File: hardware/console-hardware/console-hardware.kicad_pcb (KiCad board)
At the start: 2 copper layers, 3 parts, among them U1 ATmega32U4-A

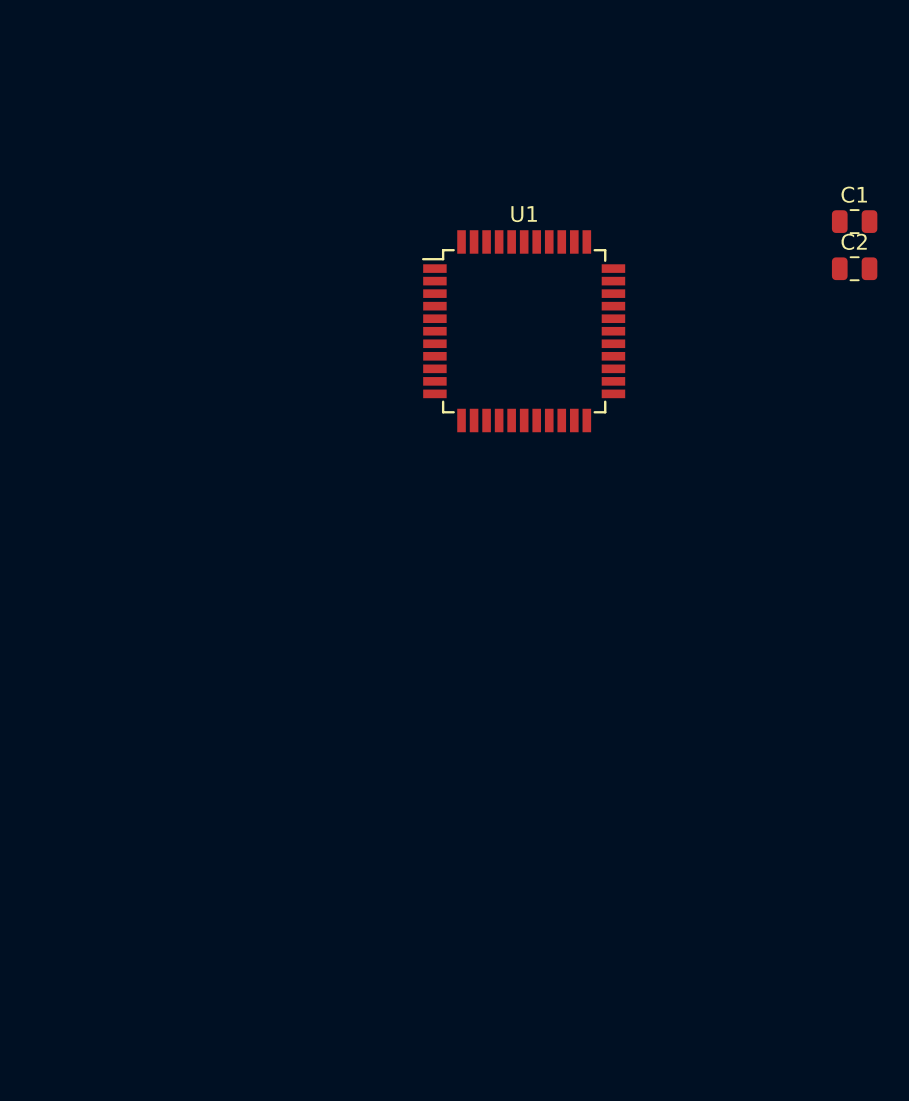
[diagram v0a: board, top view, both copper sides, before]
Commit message: Updated schematic and added preliminary layout
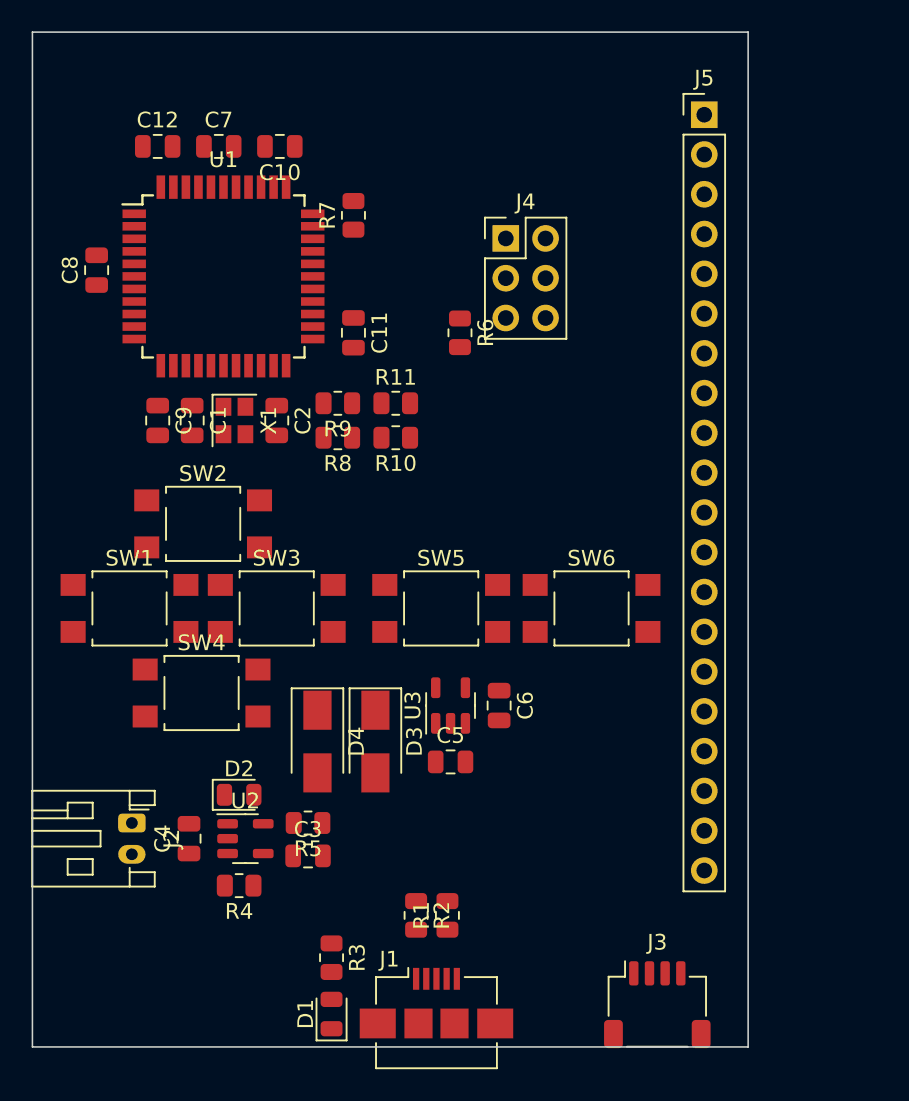
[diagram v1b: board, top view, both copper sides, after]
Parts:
- added C10: 100n, Capacitor_SMD:C_0805_2012Metric, F.Cu at (98.2, 63.7)
- added C11: 100n, Capacitor_SMD:C_0805_2012Metric, F.Cu at (102.9, 75.6)
- added C12: 100n, Capacitor_SMD:C_0805_2012Metric, F.Cu at (90.4, 63.7)
- added C3: 4.7u, Capacitor_SMD:C_0805_2012Metric, F.Cu at (100.0, 109.0)
- added C4: 4.7u, Capacitor_SMD:C_0805_2012Metric, F.Cu at (92.4, 107.9)
- added C5: 4.7u, Capacitor_SMD:C_0805_2012Metric, F.Cu at (109.1, 103.0)
- added C6: 470p, Capacitor_SMD:C_0805_2012Metric, F.Cu at (112.2, 99.4)
- added C7: 100n, Capacitor_SMD:C_0805_2012Metric, F.Cu at (94.3, 63.7)
- added C8: 1u, Capacitor_SMD:C_0805_2012Metric, F.Cu at (86.5, 71.6)
- added C9: 100n, Capacitor_SMD:C_0805_2012Metric, F.Cu at (90.4, 81.2)
- added D1: Green, LED_SMD:LED_0805_2012Metric, F.Cu at (101.5, 119.1)
- added D2: Green, LED_SMD:LED_0805_2012Metric, F.Cu at (95.6, 105.1)
- added D3: B340A, Diode_SMD:D_SMA, F.Cu at (104.3, 101.7)
- added D4: B340A, Diode_SMD:D_SMA, F.Cu at (100.6, 101.7)
- added J1: USB_B_Micro, Connector_USB:USB_Micro-B_Amphenol_10104110_Horizontal, F.Cu at (108.2, 118.4)
- added J2: LiPo battery, Connector_JST:JST_PH_S2B-PH-K_1x02_P2.00mm_Horizontal, F.Cu at (88.8, 106.9)
- added J3: Conn_01x04, Connector_JST:JST_SH_SM04B-SRSS-TB_1x04-1MP_P1.00mm_Horizontal, F.Cu at (122.3, 118.5)
- added J4: ICSP, Connector_PinHeader_2.54mm:PinHeader_2x03_P2.54mm_Vertical, F.Cu at (112.6, 69.6)
- added J5: Conn_01x20, Connector_PinHeader_2.54mm:PinHeader_1x20_P2.54mm_Vertical, F.Cu at (125.3, 61.7)
- added R1: 22, Resistor_SMD:R_0805_2012Metric, F.Cu at (108.9, 112.8)
- added R10: 0, Resistor_SMD:R_0805_2012Metric, F.Cu at (105.6, 82.3)
- added R11: 0, Resistor_SMD:R_0805_2012Metric, F.Cu at (105.6, 80.1)
- added R2: 22, Resistor_SMD:R_0805_2012Metric, F.Cu at (106.9, 112.8)
- added R3: 1k, Resistor_SMD:R_0805_2012Metric, F.Cu at (101.5, 115.5)
- added R4: 1k, Resistor_SMD:R_0805_2012Metric, F.Cu at (95.6, 110.9)
- added R5: 10k, Resistor_SMD:R_0805_2012Metric, F.Cu at (100.0, 106.9)
- added R6: 10k, Resistor_SMD:R_0805_2012Metric, F.Cu at (109.7, 75.6)
- added R7: 10k, Resistor_SMD:R_0805_2012Metric, F.Cu at (102.9, 68.1)
- added R8: 4.7k, Resistor_SMD:R_0805_2012Metric, F.Cu at (101.9, 82.3)
- added R9: 4.7k, Resistor_SMD:R_0805_2012Metric, F.Cu at (101.9, 80.1)
- added SW1: SW_Push, Button_Switch_SMD:SW_SPST_TL3305A, F.Cu at (88.6, 93.2)
- added SW2: SW_Push, Button_Switch_SMD:SW_SPST_TL3305A, F.Cu at (93.3, 87.8)
- added SW3: SW_Push, Button_Switch_SMD:SW_SPST_TL3305A, F.Cu at (98.0, 93.2)
- added SW4: SW_Push, Button_Switch_SMD:SW_SPST_TL3305A, F.Cu at (93.2, 98.6)
- added SW5: SW_Push, Button_Switch_SMD:SW_SPST_TL3305A, F.Cu at (108.5, 93.2)
- added SW6: SW_Push, Button_Switch_SMD:SW_SPST_TL3305A, F.Cu at (118.1, 93.2)
- added U2: MCP73831-2-OT, Package_TO_SOT_SMD:SOT-23-5, F.Cu at (96.0, 107.9)
- added U3: MIC5219-3.3YM5, Package_TO_SOT_SMD:SOT-23-5, F.Cu at (109.1, 99.4)
- added X1: 16 MHz, Crystal:Crystal_SMD_2520-4Pin_2.5x2.0mm, F.Cu at (95.3, 81.2)
- C1, C2: value 22p -> 30p
- moved C1 44.2 mm to (92.6, 81.2), turned to -90 degrees
- moved C2 38.2 mm to (98.0, 81.2), turned to -90 degrees
- moved U1 19.5 mm to (94.6, 72.0)
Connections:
- U1 pad 10: unconnected-(U1-Pad10) -> /MOSI
- U1 pad 11: unconnected-(U1-Pad11) -> /MISO
- U1 pad 13: unconnected-(U1-Pad13) -> /~{RESET}
- U1 pad 15: Net-(U1-Pad15) -> GND
- U1 pad 18: unconnected-(U1-Pad18) -> /SCL
- U1 pad 19: unconnected-(U1-Pad19) -> /SDA
- U1 pad 2: unconnected-(U1-Pad2) -> VBUS
- U1 pad 23: Net-(U1-Pad15) -> GND
- U1 pad 24: Net-(U1-Pad24) -> +3.3V
- U1 pad 33: unconnected-(U1-Pad33) -> Net-(R7-Pad2)
- U1 pad 35: Net-(U1-Pad15) -> GND
- U1 pad 36: unconnected-(U1-Pad36) -> Net-(SW6-Pad1)
- U1 pad 37: unconnected-(U1-Pad37) -> Net-(SW5-Pad1)
- U1 pad 38: unconnected-(U1-Pad38) -> Net-(SW4-Pad1)
- U1 pad 39: unconnected-(U1-Pad39) -> Net-(SW3-Pad1)
- U1 pad 40: unconnected-(U1-Pad40) -> Net-(SW2-Pad1)
- U1 pad 41: unconnected-(U1-Pad41) -> Net-(SW1-Pad1)
- U1 pad 42: unconnected-(U1-Pad42) -> Net-(C7-Pad1)
- U1 pad 43: Net-(U1-Pad15) -> GND
- U1 pad 44: Net-(U1-Pad24) -> +3.3V
- U1 pad 5: unconnected-(U1-Pad5) -> GND
- U1 pad 6: unconnected-(U1-Pad6) -> Net-(C8-Pad1)
- U1 pad 7: unconnected-(U1-Pad7) -> VBUS
- U1 pad 9: unconnected-(U1-Pad9) -> /SCK
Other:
- board outline added: 45.7 x 64.8 mm

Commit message: Updated schematic and layout. Added BOM
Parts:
- added D5: Green, LED_SMD:LED_0805_2012Metric, F.Cu at (108.5, 100.6)
- added JP1: Jumper_2_Open, Jumper:SolderJumper-2_P1.3mm_Open_Pad1.0x1.5mm, F.Cu at (114.6, 58.3)
- added R12: 4.7k, Resistor_SMD:R_0805_2012Metric, F.Cu at (108.5, 96.8)
- added R13: 10k, Resistor_SMD:R_0805_2012Metric, F.Cu at (84.7, 85.6)
- added R14: 10k, Resistor_SMD:R_0805_2012Metric, F.Cu at (89.3, 85.6)
- added R15: 10k, Resistor_SMD:R_0805_2012Metric, F.Cu at (101.8, 85.6)
- added R16: 10k, Resistor_SMD:R_0805_2012Metric, F.Cu at (87.0, 85.6)
- added R17: 10k, Resistor_SMD:R_0805_2012Metric, F.Cu at (104.2, 85.6)
- added R18: 10k, Resistor_SMD:R_0805_2012Metric, F.Cu at (106.6, 85.6)
- added REF**: PinHeader_1x20_P2.54mm_Vertical, Connector_PinHeader_2.54mm:PinHeader_1x20_P2.54mm_Vertical, F.Cu at (194.1, 63.9)
- added SW7: SW_SPDT, Button_Switch_THT:SW_E-Switch_EG1224_SPDT_Angled, F.Cu at (92.9, 115.6)
- R3, R4: value 1k -> 4.7k
- moved SW6 96.3 mm to (214.4, 92.6)
- moved SW5 93.8 mm to (202.3, 92.6)
- moved R10 72.8 mm to (171.8, 112.7), turned to 90 degrees
- moved R11 71.6 mm to (169.4, 112.7), turned to -90 degrees
- moved J3 47.3 mm to (169.6, 118.7)
- moved R1 45.5 mm to (154.4, 113.2)
- moved J1 45.3 mm to (153.5, 118.4)
- moved R2 45.1 mm to (152.0, 113.2)
- moved R3 44.4 mm to (145.8, 118.1)
- moved D1 41.9 mm to (143.4, 118.1), turned to -90 degrees
- moved R8 30.6 mm to (128.2, 97.9), turned to -90 degrees
- moved R9 29.5 mm to (128.2, 93.5), turned to 90 degrees
- moved C9 18.0 mm to (107.8, 76.5), turned to 0 degrees
- moved R6 17.5 mm to (112.2, 58.3), turned to 90 degrees
- moved C1 16.7 mm to (107.8, 74.3), turned to 0 degrees
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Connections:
- net Net-(J3-Pad3) renamed /SDA_OUT
- net Net-(J3-Pad4) renamed /SCL_OUT
- J5 pad 1: unconnected-(J5-Pad1) -> +3.3V
- J5 pad 10: unconnected-(J5-Pad10) -> /DISPLAY_LITE
- J5 pad 11: unconnected-(J5-Pad11) -> GND
- J5 pad 12: unconnected-(J5-Pad12) -> /DISPLAY_IRQ
- J5 pad 13: unconnected-(J5-Pad13) -> /SDA
- J5 pad 14: unconnected-(J5-Pad14) -> /SCL
- J5 pad 2: unconnected-(J5-Pad2) -> GND
- J5 pad 3: +3.3V -> /3VO
- J5 pad 4: GND -> /SCK
- J5 pad 5: unconnected-(J5-Pad5) -> /MISO
- J5 pad 6: unconnected-(J5-Pad6) -> /MOSI
- J5 pad 7: unconnected-(J5-Pad7) -> /DISPLAY_CS
- J5 pad 8: unconnected-(J5-Pad8) -> /DISPLAY_DC
- J5 pad 9: unconnected-(J5-Pad9) -> /DISPLAY_RST
- U1 pad 12: unconnected-(U1-Pad12) -> /DISPLAY_IRQ
- U1 pad 27: unconnected-(U1-Pad27) -> /DISPLAY_CS
- U1 pad 28: unconnected-(U1-Pad28) -> /DISPLAY_DC
- U1 pad 29: unconnected-(U1-Pad29) -> /DISPLAY_RST
- U1 pad 30: unconnected-(U1-Pad30) -> /DISPLAY_LITE
- U3 pad 3: unconnected-(U3-Pad3) -> /ON/~{OFF}
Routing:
- net +3.3V: track 0.00 -> 155.4 mm, vias 0 -> 7
- net Net-(R18-Pad2): track 0.00 -> 153.6 mm, vias 0 -> 3
- net Net-(R17-Pad2): track 0.00 -> 142.4 mm, vias 0 -> 3
- net VBUS: track 0.00 -> 112.8 mm, vias 0 -> 2
- net /SCL: track 0.00 -> 98.2 mm, vias 0 -> 1
- net /SDA: track 0.00 -> 95.3 mm, vias 0 -> 1
- net /RD+: track 0.00 -> 94.7 mm
- net /RD-: track 0.00 -> 93.1 mm
- net /DISPLAY_LITE: track 0.00 -> 53.7 mm
- net /DISPLAY_RST: track 0.00 -> 48.5 mm
- net Net-(R16-Pad2): track 0.00 -> 45.6 mm, vias 0 -> 2
- net /DISPLAY_DC: track 0.00 -> 43.3 mm
- net /DISPLAY_CS: track 0.00 -> 38.1 mm
- net Net-(R15-Pad2): track 0.00 -> 34.4 mm, vias 0 -> 2
- net Net-(R13-Pad2): track 0.00 -> 31.0 mm, vias 0 -> 2
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- added copper zone on B.Cu, net GND
- added copper zone on F.Cu, net GND
- added copper zone on F.Cu, net VBUS
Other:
- board size 45.7 x 64.8 mm -> 140 x 64.8 mm
- board text added: "BATTERY"
- board text added: "CHARGING"
- board text added: "I2C ACCESSORIES"
- board text added: "ON/OFF"
- board text added: "POWER IN"
- board text added: "POWER SWITCH"
- board text added: "RESET"

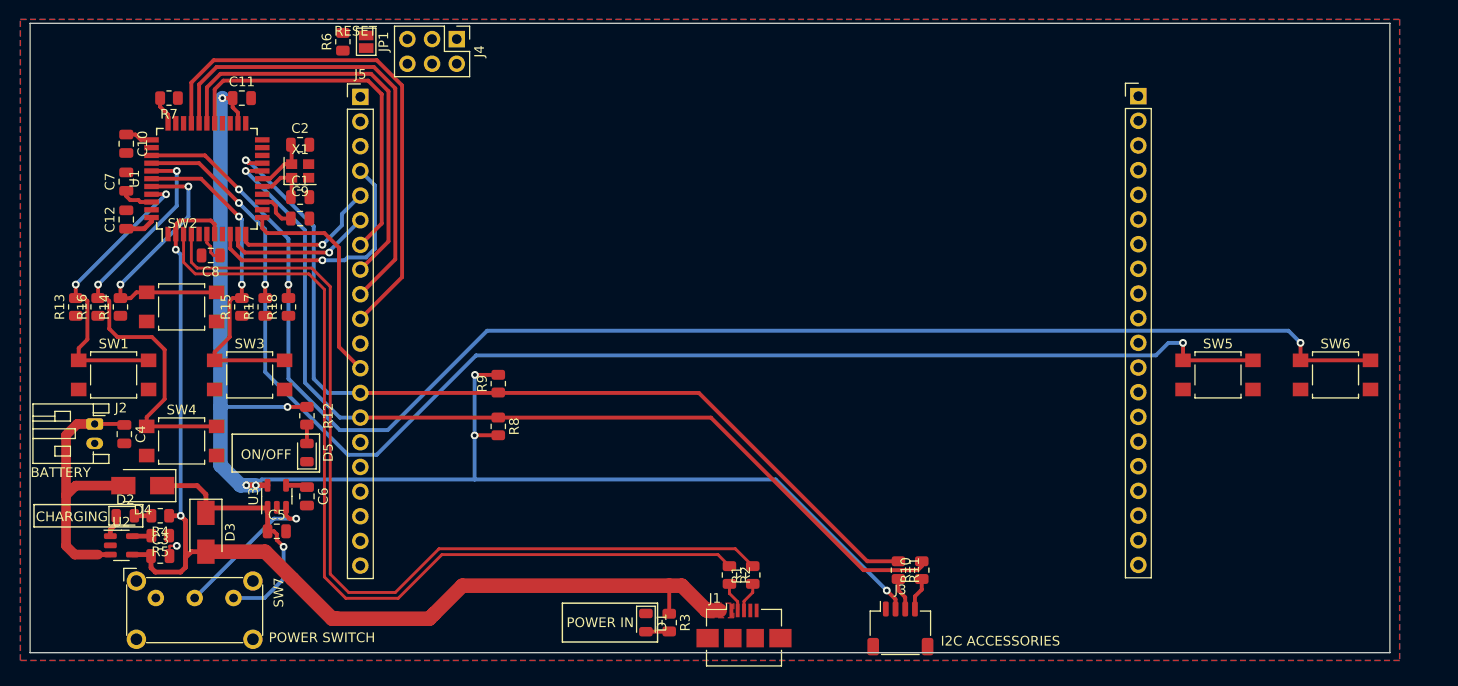
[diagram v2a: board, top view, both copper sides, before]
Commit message: Updated board layout, some small schematic fixes, and added 3D models
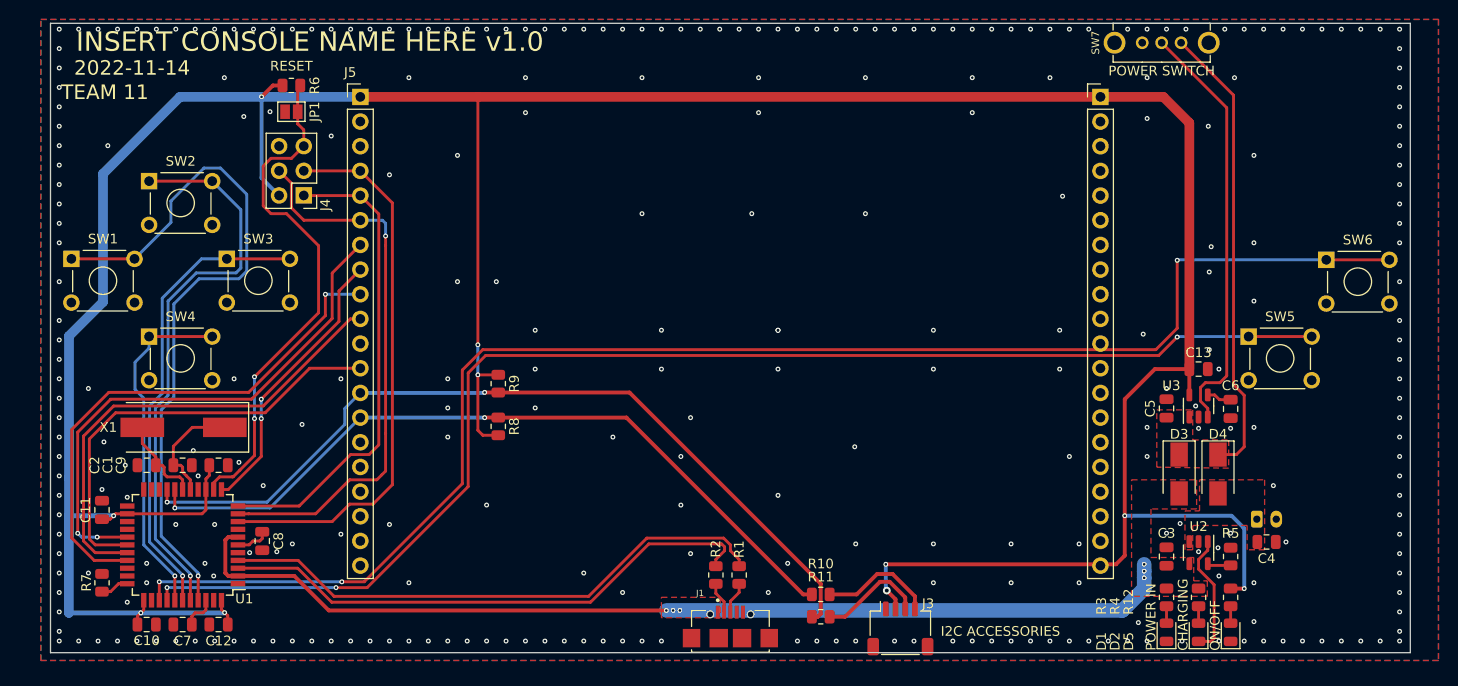
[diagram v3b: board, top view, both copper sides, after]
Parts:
- removed R13, R14, R15, R16, R17, R18: 10k, Resistor_SMD:R_0805_2012Metric
- added C13: 4.7u, Capacitor_SMD:C_0805_2012Metric, F.Cu at (200.3, 92.0)
- J1: footprint Connector_USB:USB_Micro-B_Amphenol_10104110_Horizontal -> USB-Conn:WE_629105136821
- J2: moved to B.Cu
- SW1, SW2, SW3, SW4, SW5, SW6: footprint Button_Switch_SMD:SW_SPST_TL3305A -> Button_Switch_THT:SW_TH_Tactile_Omron_B3F-10xx
- SW7: footprint Button_Switch_THT:SW_E-Switch_EG1224_SPDT_Angled -> SW-EG1213:SW_EG1213
- X1: footprint Crystal:Crystal_SMD_2520-4Pin_2.5x2.0mm -> Crystal:Crystal_SMD_HC49-SD
- moved J2 120.1 mm to (206.3, 107.5), turned to 0 degrees
- moved SW7 118.3 mm to (196.5, 58.4)
- moved C4 118.1 mm to (207.3, 109.8), turned to 0 degrees
- moved D2 111.1 mm to (200.3, 119.1), turned to 90 degrees
- moved U2 110.9 mm to (200.3, 110.9), turned to -90 degrees
- moved D4 110.7 mm to (202.3, 102.8), turned to -90 degrees
- moved R5 110.2 mm to (203.6, 111.3), turned to -90 degrees
- moved R4 107.2 mm to (200.3, 115.5), turned to -90 degrees
- moved C3 103.6 mm to (197.0, 111.3), turned to 90 degrees
- moved D3 100.4 mm to (198.3, 102.8)
- moved R12 96.9 mm to (203.6, 115.5)
- moved D5 96.9 mm to (203.6, 119.1)
- moved C6 95.5 mm to (203.6, 96.1)
- moved U3 95.4 mm to (200.3, 95.8)
- moved C5 92.5 mm to (197.0, 96.0), turned to 90 degrees
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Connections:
- J3 pad MP: (no net) -> GND
- U1 pad 12: /DISPLAY_IRQ -> /DISPLAY_DC
- U1 pad 28: /DISPLAY_DC -> /DISPLAY_IRQ
- U1 pad 29: /DISPLAY_RST -> /DISPLAY_LITE
- U1 pad 30: /DISPLAY_LITE -> /DISPLAY_RST
- X1 pad 2: GND -> Net-(C2-Pad1)
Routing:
- net +3.3V: track 155.4 -> 359.8 mm, vias 7 -> 10
- net /~{RESET}: track 0.00 -> 53.5 mm, vias 0 -> 2
- net Net-(SW1-Pad1): track 31.0 -> 73.8 mm, vias 2 -> 1
- net /MOSI: track 15.5 -> 57.2 mm
- net /RD+: track 94.7 -> 57.6 mm
- net /RD-: track 93.1 -> 56.5 mm
- net /MISO: track 15.5 -> 49.4 mm, vias 1 -> 0
- net /SCK: track 26.0 -> 57.0 mm, vias 1 -> 0
- net Net-(SW2-Pad1): track 28.3 -> 58.4 mm, vias 2 -> 1
- net +BATT: track 29.2 -> 0.00 mm
- net /ON/~{OFF}: track 15.8 -> 43.6 mm, vias 1 -> 0
- net /DISPLAY_IRQ: track 23.2 -> 45.4 mm
- net Net-(C5-Pad1): track 27.8 -> 47.3 mm, vias 1 -> 0
- net /SCL: track 98.2 -> 78.9 mm, vias 1 -> 2
- net /DISPLAY_CS: track 38.1 -> 55.5 mm, vias 0 -> 2
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- added copper zone on F.Cu, net +BATT
- added copper zone on F.Cu, net Net-(C5-Pad1)
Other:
- rule pad_to_mask_clearance: 0 -> 0.0508
- board text added: "2022-11-14"
- board text added: "INSERT CONSOLE NAME HERE v1.0"
- board text added: "TEAM 11"

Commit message: Updated board, fixed drc errors, added mounting holes and test points, added name
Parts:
- added REF**: MountingHole_2.2mm_M2, MountingHole:MountingHole_2.2mm_M2, F.Cu at (84.6, 58.9)
- added REF**: MountingHole_2.2mm_M2, MountingHole:MountingHole_2.2mm_M2, F.Cu at (219.6, 118.7)
- added REF**: MountingHole_2.2mm_M2, MountingHole:MountingHole_2.2mm_M2, F.Cu at (219.6, 58.9)
- added REF**: MountingHole_2.2mm_M2, MountingHole:MountingHole_2.2mm_M2, F.Cu at (84.6, 118.7)
- added TP1: Test-Point, Testpoints:1X01, F.Cu at (142.9, 118.8)
- added TP10: Test-Point, Testpoints:1X01, F.Cu at (116.6, 84.3)
- added TP11: Test-Point, Testpoints:1X01, F.Cu at (116.6, 79.2)
- added TP12: Test-Point, Testpoints:1X01, F.Cu at (116.6, 86.8)
- added TP13: Test-Point, Testpoints:1X01, F.Cu at (116.6, 91.9)
- added TP14: Test-Point, Testpoints:1X01, F.Cu at (87.0, 103.9)
- added TP15: Test-Point, Testpoints:1X01, F.Cu at (88.6, 103.9)
- added TP16: Test-Point, Testpoints:1X01, F.Cu at (90.2, 103.9)
- added TP2: Test-Point, Testpoints:1X01, F.Cu at (142.9, 116.9)
- added TP3: Test-Point, Testpoints:1X01, F.Cu at (206.4, 112.1)
- added TP4: Test-Point, Testpoints:1X01, F.Cu at (196.7, 98.5)
- added TP5: Test-Point, Testpoints:1X01, F.Cu at (200.9, 62.8)
- added TP6: Test-Point, Testpoints:1X01, F.Cu at (199.4, 87.0)
- added TP7: Test-Point, Testpoints:1X01, F.Cu at (120.5, 97.0)
- added TP8: Test-Point, Testpoints:1X01, F.Cu at (120.5, 94.5)
- added TP9: Test-Point, Testpoints:1X01, F.Cu at (116.6, 81.8)
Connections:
- J5 pad 1: +3.3V -> GND
- J5 pad 2: GND -> +3.3V
- U1 pad 20: unconnected-(U1-Pad20) -> Net-(U1-Pad20)
- U1 pad 21: unconnected-(U1-Pad21) -> Net-(U1-Pad21)
- U1 pad 22: unconnected-(U1-Pad22) -> Net-(U1-Pad22)
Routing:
- net Net-(U1-Pad20): track 0.00 -> 7.90 mm
- net Net-(U1-Pad21): track 0.00 -> 5.55 mm
- net Net-(SW6-Pad1): track 153.2 -> 149.1 mm
- net /DISPLAY_RST: track 54.6 -> 57.2 mm
- net /DISPLAY_DC: track 29.0 -> 31.6 mm
- net /DISPLAY_CS: track 55.5 -> 58.1 mm
- net /DISPLAY_LITE: track 49.3 -> 51.9 mm
- net /DISPLAY_IRQ: track 45.4 -> 48.0 mm
- net Net-(U1-Pad22): track 0.00 -> 1.71 mm
- net /SCK: track 57.0 -> 58.6 mm
- net /MOSI: track 57.2 -> 58.9 mm
- net /MISO: track 49.4 -> 51.0 mm
- net +3.3V: track 359.8 -> 358.8 mm
- net GND: vias 300 -> 301
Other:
- board text added: "Nerd Box v1.0"
- board text removed: "INSERT CONSOLE NAME HERE v1.0"

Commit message: Finishing touches to the PCB. Updated attributes for parts.
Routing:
- net Net-(SW6-Pad1): track 149.1 -> 146.8 mm
- net +BATT: track 0.00 -> 2.32 mm
- net GND: vias 301 -> 332
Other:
- board text added: "2022-11-16"
- board text removed: "2022-11-14"
